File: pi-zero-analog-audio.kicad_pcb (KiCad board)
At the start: 2 copper layers, 65 x 30 mm, 5 parts, among them J1 GPIO

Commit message: Unrouted
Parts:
- added C1: 1u, Capacitor_SMD:C_0805_2012Metric_Pad1.18x1.45mm_HandSolder, F.Cu at (142.9, 78.4)
- added C2: 4.7u, Capacitor_SMD:C_0805_2012Metric_Pad1.18x1.45mm_HandSolder, F.Cu at (143.2, 85.3)
- added C3: 47u, Capacitor_SMD:C_0805_2012Metric_Pad1.18x1.45mm_HandSolder, F.Cu at (154.4, 86.0)
- added C4: 100n, Capacitor_SMD:C_0805_2012Metric_Pad1.18x1.45mm_HandSolder, F.Cu at (155.9, 78.3)
- added C5: 100n, Capacitor_SMD:C_0805_2012Metric_Pad1.18x1.45mm_HandSolder, F.Cu at (151.6, 84.5)
- added C6: 47u, Capacitor_SMD:C_0805_2012Metric_Pad1.18x1.45mm_HandSolder, F.Cu at (146.5, 86.0)
- added C7: 100n, Capacitor_SMD:C_0805_2012Metric_Pad1.18x1.45mm_HandSolder, F.Cu at (147.2, 78.3)
- added J2: SJ1-3555NG-BE, kicad_fridrich:CUI_SJ1-3555NG-BE, F.Cu at (151.6, 97.0)
- added R1: 220R, Resistor_SMD:R_0805_2012Metric_Pad1.20x1.40mm_HandSolder, F.Cu at (155.9, 82.9)
- added R2: 100R, Resistor_SMD:R_0805_2012Metric_Pad1.20x1.40mm_HandSolder, F.Cu at (155.9, 80.6)
- added R3: 1.8k, Resistor_SMD:R_0805_2012Metric_Pad1.20x1.40mm_HandSolder, F.Cu at (156.6, 86.0)
- added R4: 220R, Resistor_SMD:R_0805_2012Metric_Pad1.20x1.40mm_HandSolder, F.Cu at (147.2, 82.9)
- added R5: 100R, Resistor_SMD:R_0805_2012Metric_Pad1.20x1.40mm_HandSolder, F.Cu at (147.2, 80.6)
- added R6: 1.8k, Resistor_SMD:R_0805_2012Metric_Pad1.20x1.40mm_HandSolder, F.Cu at (148.8, 86.0)
- added U1: LP5907MFX-3.3, Package_TO_SOT_SMD:SOT-23-5, F.Cu at (142.9, 82.0)
- added U2: 74LVC2G34, Package_TO_SOT_SMD:SOT-23-6_Handsoldering, F.Cu at (151.6, 79.7)
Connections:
- net +3V3 renamed +3.3V
- J1 pad 10: /GPIO[15]/RXD0 -> unconnected-(J1-Pad10)
- J1 pad 11: /GPIO[17] -> unconnected-(J1-Pad11)
- J1 pad 12: /GPIO[18]/PCM.CLK -> unconnected-(J1-Pad12)
- J1 pad 13: /GPIO[27] -> unconnected-(J1-Pad13)
- J1 pad 15: /GPIO[22] -> unconnected-(J1-Pad15)
- J1 pad 16: /GPIO[23] -> unconnected-(J1-Pad16)
- J1 pad 18: /GPIO[24] -> unconnected-(J1-Pad18)
- J1 pad 19: /GPIO[10]/SPI0.MOSI -> unconnected-(J1-Pad19)
- J1 pad 21: /GPIO[9]/SPI0.MISO -> unconnected-(J1-Pad21)
- J1 pad 22: /GPIO[25] -> unconnected-(J1-Pad22)
- J1 pad 23: /GPIO[11]/SPI0.SCLK -> unconnected-(J1-Pad23)
- J1 pad 24: /GPIO[8]/SPI0.CE0 -> unconnected-(J1-Pad24)
- J1 pad 26: /GPIO[7]/SPI0.CE1 -> unconnected-(J1-Pad26)
- J1 pad 27: /ID_SDA -> unconnected-(J1-Pad27)
- J1 pad 28: /ID_SCL -> unconnected-(J1-Pad28)
- J1 pad 29: /GPIO[5] -> unconnected-(J1-Pad29)
- J1 pad 3: /GPIO[2]/SDA1 -> unconnected-(J1-Pad3)
- J1 pad 31: /GPIO[6] -> unconnected-(J1-Pad31)
- J1 pad 32: /GPIO[12]/PWM0 -> /PWM0
- J1 pad 33: /GPIO[13]/PWM1 -> /PWM1
- J1 pad 35: /GPIO[19]/PCM.FS -> unconnected-(J1-Pad35)
- J1 pad 36: /GPIO[16] -> unconnected-(J1-Pad36)
- J1 pad 37: /GPIO26 -> unconnected-(J1-Pad37)
- J1 pad 38: /GPIO[20]/PCM.DIN -> unconnected-(J1-Pad38)
- J1 pad 40: /GPIO[21]/PCM.DOUT -> unconnected-(J1-Pad40)
- J1 pad 5: /GPIO[3]/SCL1 -> unconnected-(J1-Pad5)
- J1 pad 7: /GPIO[4]/GPCLK0 -> unconnected-(J1-Pad7)
- J1 pad 8: /GPIO[14]/TXD0 -> unconnected-(J1-Pad8)
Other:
- board text added: "E"
- board text removed: "Extend PCB edge 0.5mm if using SMT header"

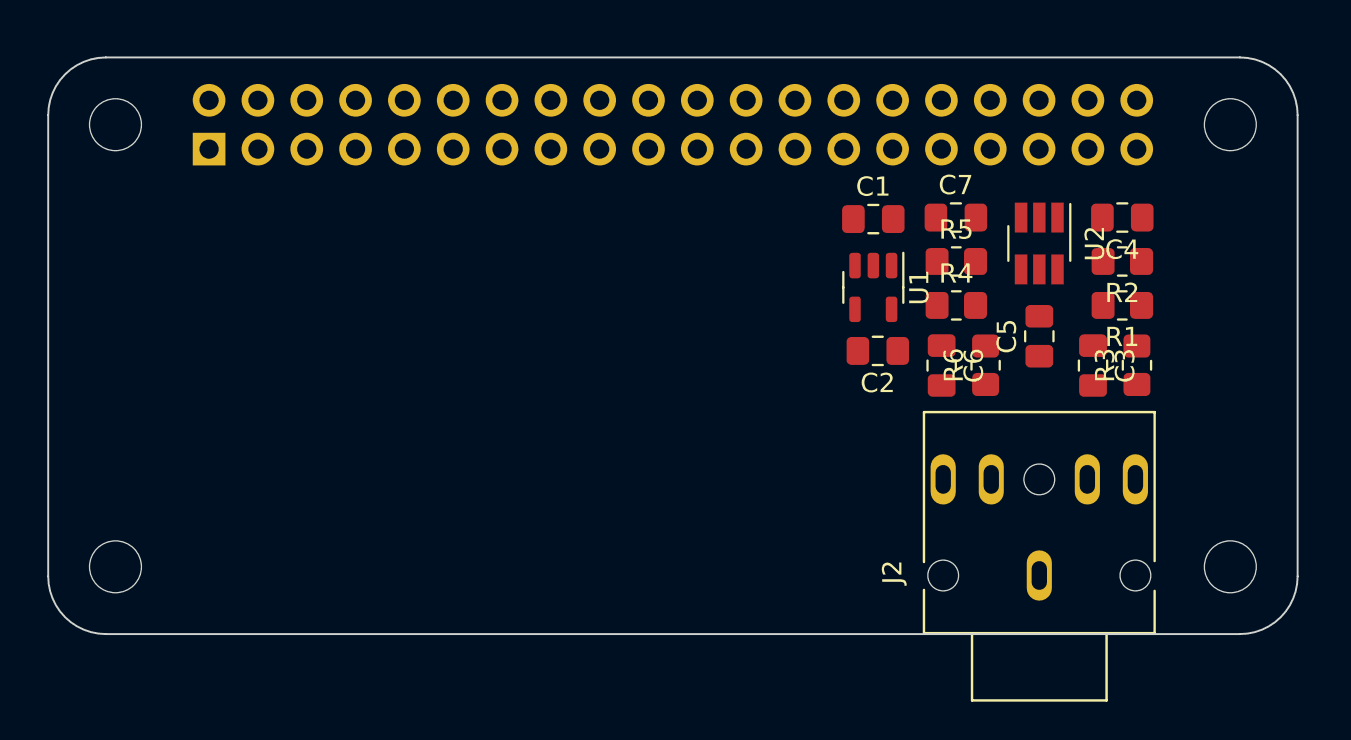
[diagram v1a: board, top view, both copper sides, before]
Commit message: we are using internal symbol libraries
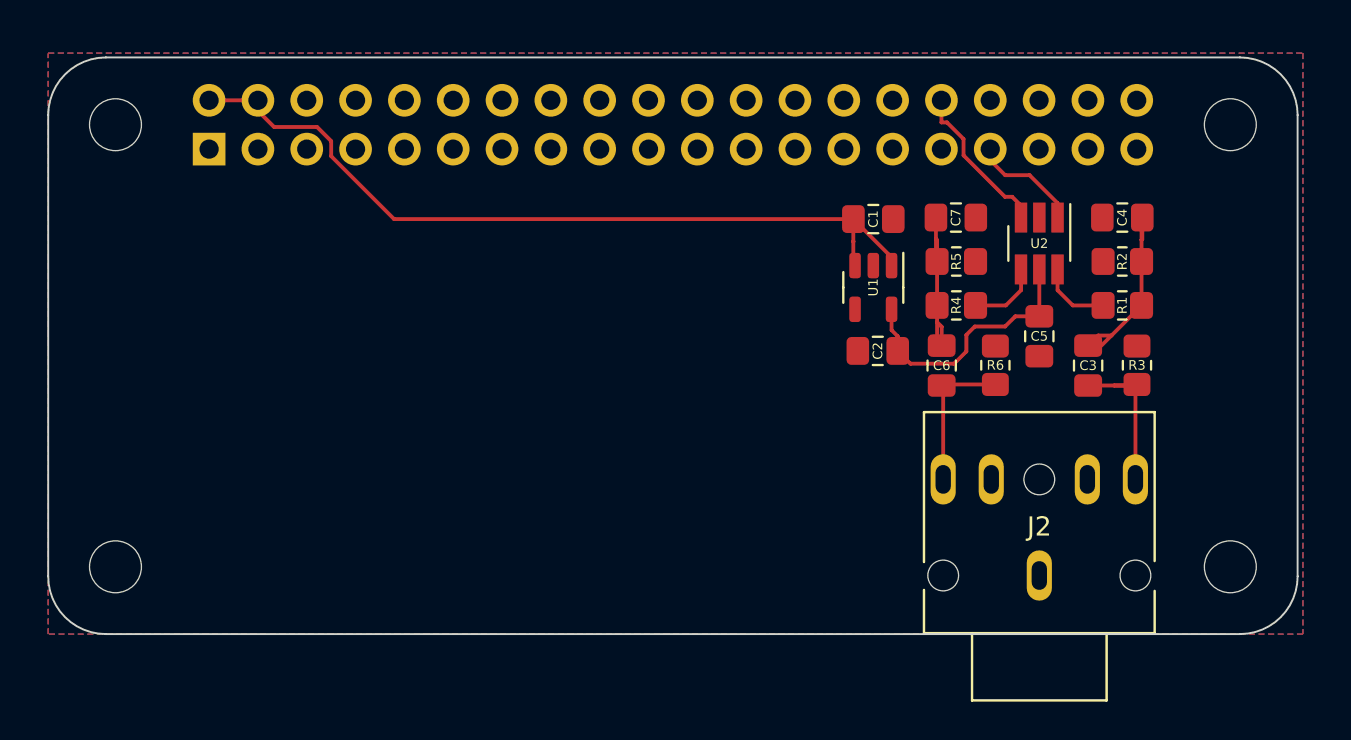
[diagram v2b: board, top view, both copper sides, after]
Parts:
- J2: footprint kicad_fridrich:CUI_SJ1-3555NG-BE -> library:CUI_SJ1-3555NG-BE
- moved R6 0.51 mm to (149.3, 86.0)
- moved C3 0.25 mm to (154.1, 86.0)
- turned C5 to -90 degrees
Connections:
- J1 pad 1: +3.3V -> unconnected-(J1-Pad1)
- J1 pad 17: +3.3V -> unconnected-(J1-Pad17)
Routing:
- net +5V: track 0.00 -> 41.1 mm
- net VCC: track 0.00 -> 13.9 mm
- net Net-(C3-Pad1): track 0.00 -> 8.98 mm
- net Net-(C6-Pad1): track 0.00 -> 8.77 mm
- net /AUDIO_L: track 0.00 -> 8.20 mm
- net /PWM0: track 0.00 -> 7.59 mm
- net /AUDIO_R: track 0.00 -> 6.86 mm
- net /PWM1: track 0.00 -> 5.17 mm
- net Net-(R4-Pad2): track 0.00 -> 3.78 mm
- net Net-(R1-Pad2): track 0.00 -> 3.78 mm
- added copper zone on B.Cu, net GND
- added copper zone on F.Cu, net GND
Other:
- board text removed: "E"
- board text removed: "PoE"

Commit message: Another day starts
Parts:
- added C8: 470u, Capacitor_THT:CP_Radial_D8.0mm_P3.50mm, F.Cu at (140.4, 92.4)
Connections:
- J2 pad 4: unconnected-(J2-Pad4) -> /AMP_L
- J2 pad 5: unconnected-(J2-Pad5) -> /AMP_R
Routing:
- net +5V: track 41.1 -> 0.00 mm
- net GND: track 0.00 -> 22.0 mm, vias 0 -> 6
- net VCC: track 13.9 -> 16.9 mm
- net Net-(C6-Pad1): track 8.77 -> 6.37 mm
- net /PWM0: track 7.59 -> 8.48 mm
- net /AUDIO_L: track 8.20 -> 7.34 mm
- net Net-(C3-Pad1): track 8.98 -> 8.18 mm
- net /PWM1: track 5.17 -> 5.75 mm
- net /AUDIO_R: track 6.86 -> 7.39 mm
- added copper zone on F.Cu, net +5V
- removed copper zone on F.Cu, net GND

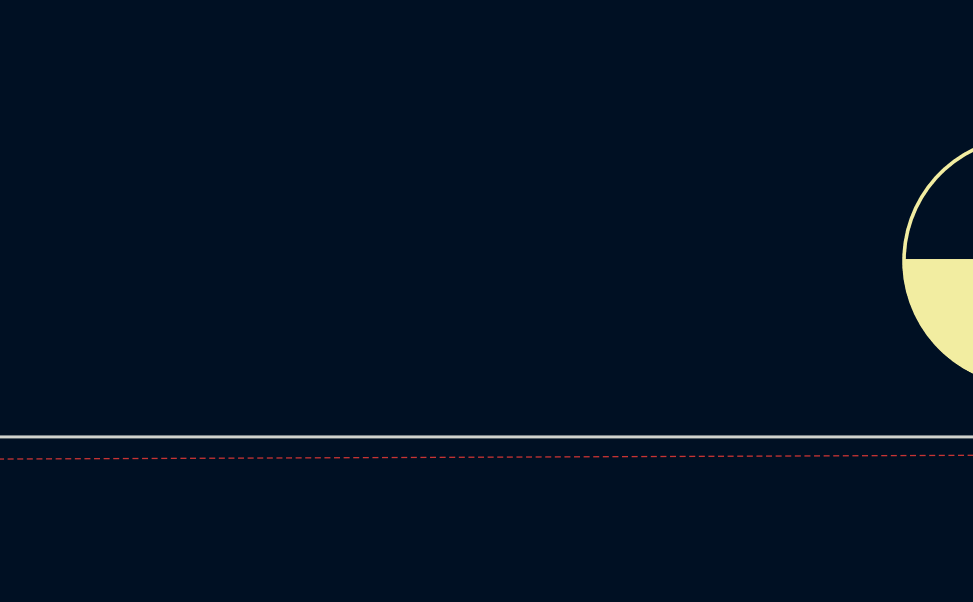
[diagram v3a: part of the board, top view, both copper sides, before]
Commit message: Adding a connector for a possible Class-D amplifier
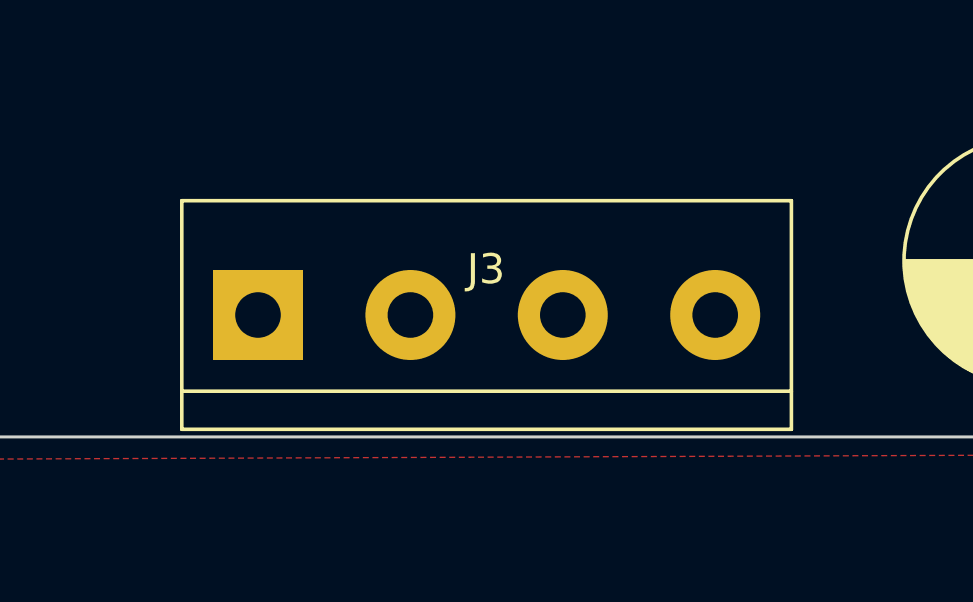
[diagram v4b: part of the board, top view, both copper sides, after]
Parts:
- added J3: Screw_Terminal_01x04, TerminalBlock:TerminalBlock_bornier-4_P5.08mm, F.Cu at (114.7, 95.9)
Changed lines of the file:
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@@
   (net 41 "unconnected-(J1-Pad17)")
   (net 42 "/AMP_R")
+  (net 43 "unconnected-(J3-Pad1)")
+  (net 44 "unconnected-(J3-Pad2)")
+  (net 45 "unconnected-(J3-Pad3)")
+  (net 46 "unconnected-(J3-Pad4)")
   (footprint "library:CUI_SJ1-3555NG-BE" (layer "F.Cu")
     (at 151.562 96.952 90)
@@
     )
   )
+  (footprint "TerminalBlock:TerminalBlock_bornier-4_P5.08mm" (layer "F.Cu")
+    (at 114.732 95.936)
+    (descr "simple 4-pin terminal block, pitch 5.08mm, revamped version of bornier4")
+    (tags "terminal block bornier4")
+    (property "Sheetfile" "pi-zero-analog-audio.kicad_sch")
+    (property "Sheetname" "")
+    (attr through_hole)
+    (fp_text reference "J3" (at 7.6 -1.524) (layer "F.SilkS")
+      (effects (font (size 1 1) (thickness 0.15)))
+    )
+    (fp_text value "Screw_Terminal_01x04" (at 7.6 4.75) (layer "F.Fab")
+      (effects (font (size 1 1) (thickness 0.15)))
+    )
+    (fp_text user "${REFERENCE}" (at 7.62 0) (layer "F.Fab")
+      (effects (font (size 1 1) (thickness 0.15)))
+    )
+    (fp_line (start 17.78 3.81) (end 17.78 -3.81) (layer "F.SilkS") (width 0.12))
+    (fp_line (start -2.54 3.81) (end 17.78 3.81) (layer "F.SilkS") (width 0.12))
+    (fp_line (start -2.54 -3.81) (end -2.54 3.81) (layer "F.SilkS") (width 0.12))
+    (fp_line (start -2.54 -3.81) (end 17.78 -3.81) (layer "F.SilkS") (width 0.12))
+    (fp_line (start 17.78 2.54) (end -2.54 2.54) (layer "F.SilkS") (width 0.12))
+    (fp_line (start -2.73 -4) (end -2.73 4) (layer "F.CrtYd") (width 0.05))
+    (fp_line (start 17.97 4) (end 17.97 -4) (layer "F.CrtYd") (width 0.05))
+    (fp_line (start 17.97 4) (end -2.73 4) (layer "F.CrtYd") (width 0.05))
+    (fp_line (start -2.73 -4) (end 17.97 -4) (layer "F.CrtYd") (width 0.05))
+    (fp_line (start 17.72 -3.75) (end 17.72 3.75) (layer "F.Fab") (width 0.1))
+    (fp_line (start -2.48 2.55) (end 17.72 2.55) (layer "F.Fab") (width 0.1))
+    (fp_line (start -2.43 3.75) (end -2.48 3.75) (layer "F.Fab") (width 0.1))
+    (fp_line (start -2.48 3.75) (end -2.48 -3.75) (layer "F.Fab") (width 0.1))
+    (fp_line (start -2.48 -3.75) (end 17.72 -3.75) (layer "F.Fab") (width 0.1))
+    (fp_line (start 17.72 3.75) (end -2.43 3.75) (layer "F.Fab") (width 0.1))
+    (pad "1" thru_hole rect (at 0 0) (size 3 3) (drill 1.52) (layers *.Cu *.Mask)
+      (net 43 "unconnected-(J3-Pad1)") (pinfunction "Pin_1") (pintype "passive"))
+    (pad "2" thru_hole circle (at 5.08 0) (size 3 3) (drill 1.52) (layers *.Cu *.Mask)
+      (net 44 "unconnected-(J3-Pad2)") (pinfunction "Pin_2") (pintype "passive"))
+    (pad "3" thru_hole circle (at 10.16 0) (size 3 3) (drill 1.52) (layers *.Cu *.Mask)
+      (net 45 "unconnected-(J3-Pad3)") (pinfunction "Pin_3") (pintype "passive"))
+    (pad "4" thru_hole circle (at 15.24 0) (size 3 3) (drill 1.52) (layers *.Cu *.Mask)
+      (net 46 "unconnected-(J3-Pad4)") (pinfunction "Pin_4") (pintype "passive"))
+    (model "${KIPRJMOD}/library/connector_1x4.wrl"
+      (offset (xyz 7.5 0 0))
+      (scale (xyz 1 1 1))
+      (rotate (xyz 0 0 180))
+    )
+  )

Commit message: Evenings come with the same regularity as the mornings
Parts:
- removed J3: Screw_Terminal_01x04, TerminalBlock:TerminalBlock_bornier-4_P5.08mm
- moved C3 2.54 mm to (156.6, 86.1)
- moved R3 2.29 mm to (154.4, 86.0)
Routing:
- net Net-(C6-Pad1): track 6.37 -> 7.59 mm
- net GND: track 22.0 -> 23.1 mm
- net Net-(C3-Pad1): track 8.18 -> 7.59 mm

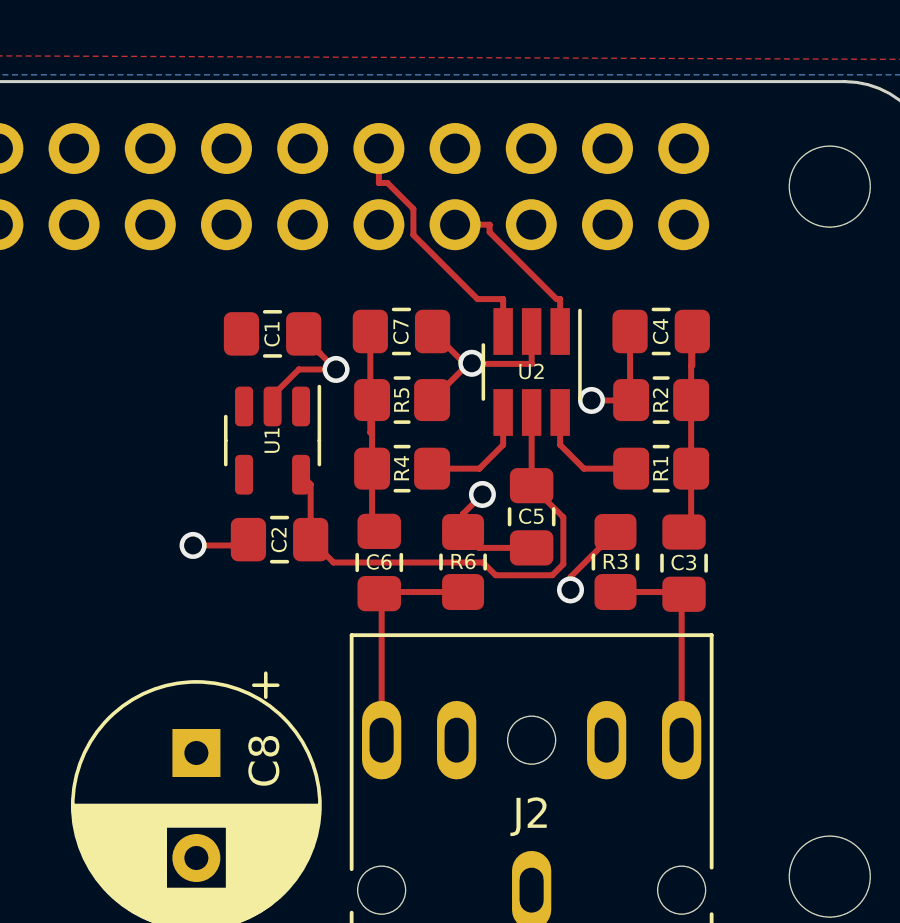
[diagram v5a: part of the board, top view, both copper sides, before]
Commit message: Trying to adapt so that sot-23 and sc-70 elements can be used in the same footprint
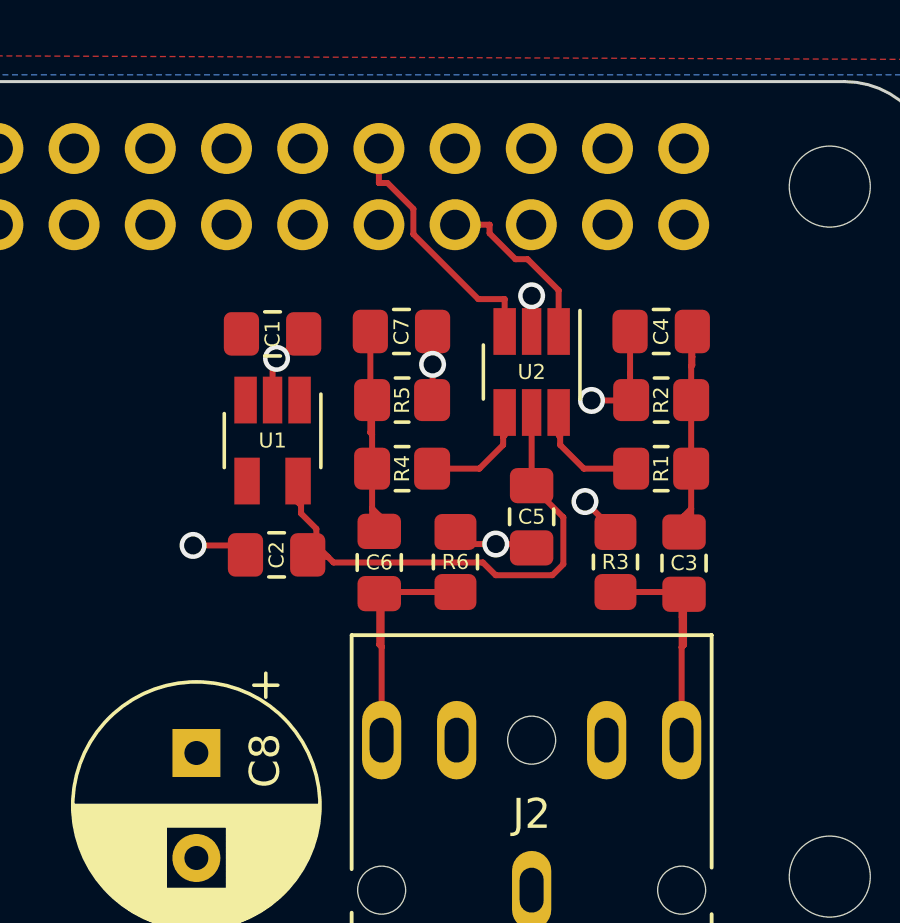
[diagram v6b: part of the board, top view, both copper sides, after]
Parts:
- U1: footprint Package_TO_SOT_SMD:SOT-23-5 -> Package_TO_SOT_SMD:SOT-23-5_HandSoldering
- moved C2 0.52 mm to (143.1, 85.8)
- moved R6 0.25 mm to (149.0, 86.0)
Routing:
- net GND: track 23.1 -> 13.5 mm, vias 6 -> 7
- net /AUDIO_L: track 6.99 -> 9.74 mm
- net /AUDIO_R: track 7.39 -> 9.08 mm
- net Net-(C6-Pad1): track 7.59 -> 8.45 mm

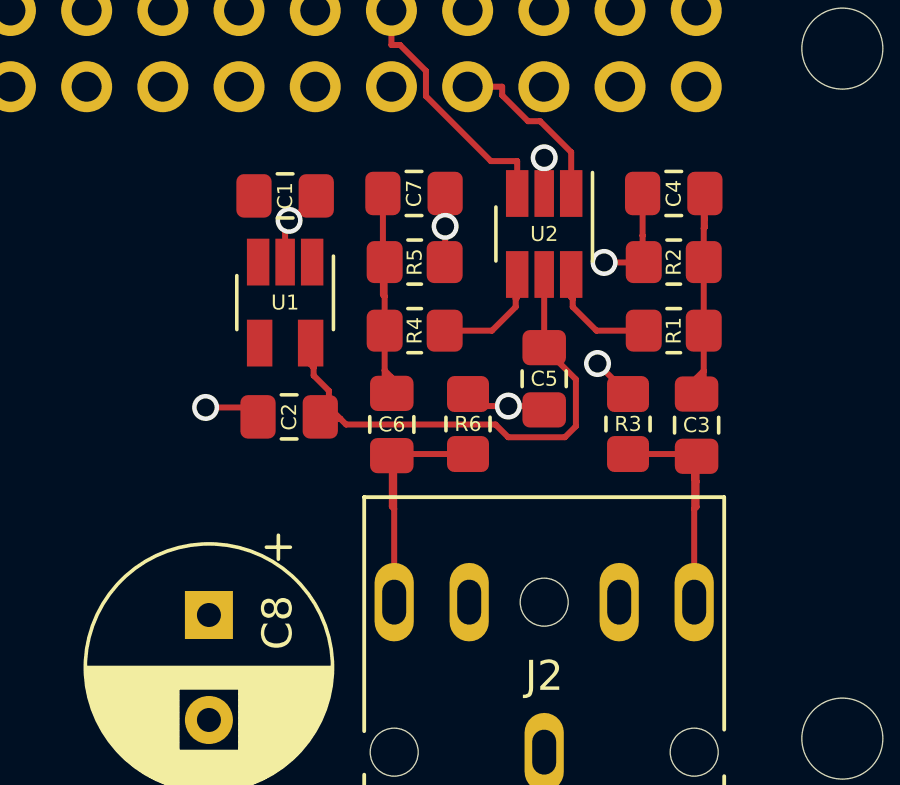
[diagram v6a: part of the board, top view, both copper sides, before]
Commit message: Vias inside the pads
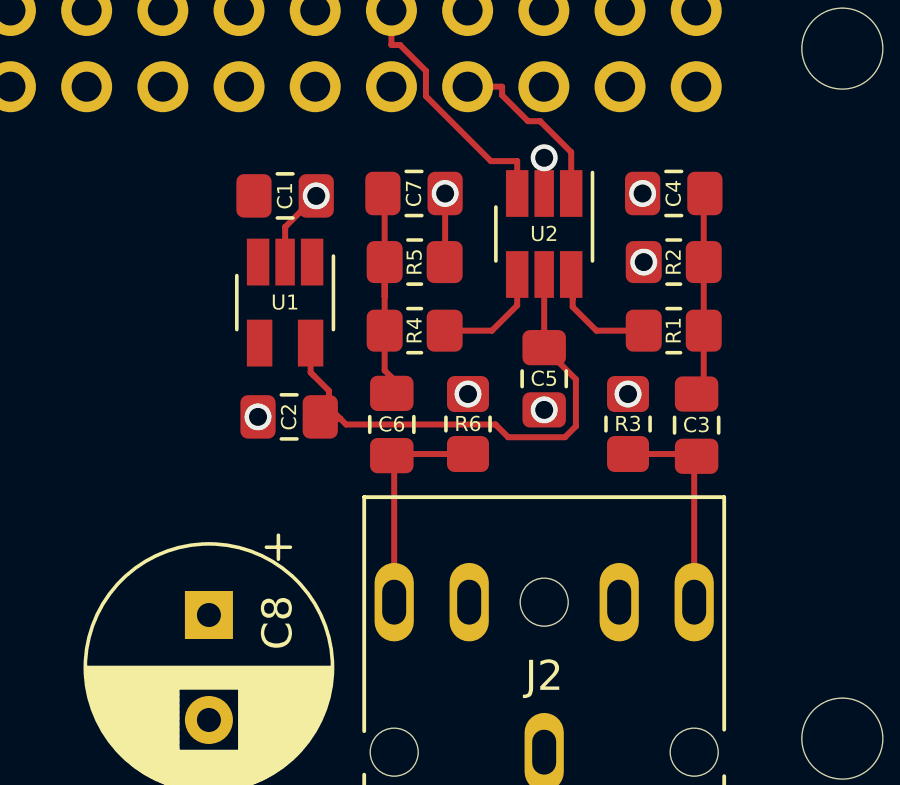
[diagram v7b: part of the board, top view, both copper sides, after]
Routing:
- net GND: track 13.5 -> 5.51 mm, vias 7 -> 9
- net /AUDIO_L: track 9.74 -> 6.99 mm
- net /AUDIO_R: track 9.08 -> 7.26 mm
- net Net-(C3-Pad1): track 7.33 -> 5.85 mm
- net Net-(R1-Pad2): track 4.07 -> 3.24 mm
- net Net-(C6-Pad1): track 8.45 -> 7.85 mm
